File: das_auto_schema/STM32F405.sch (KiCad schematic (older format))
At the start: 11 parts

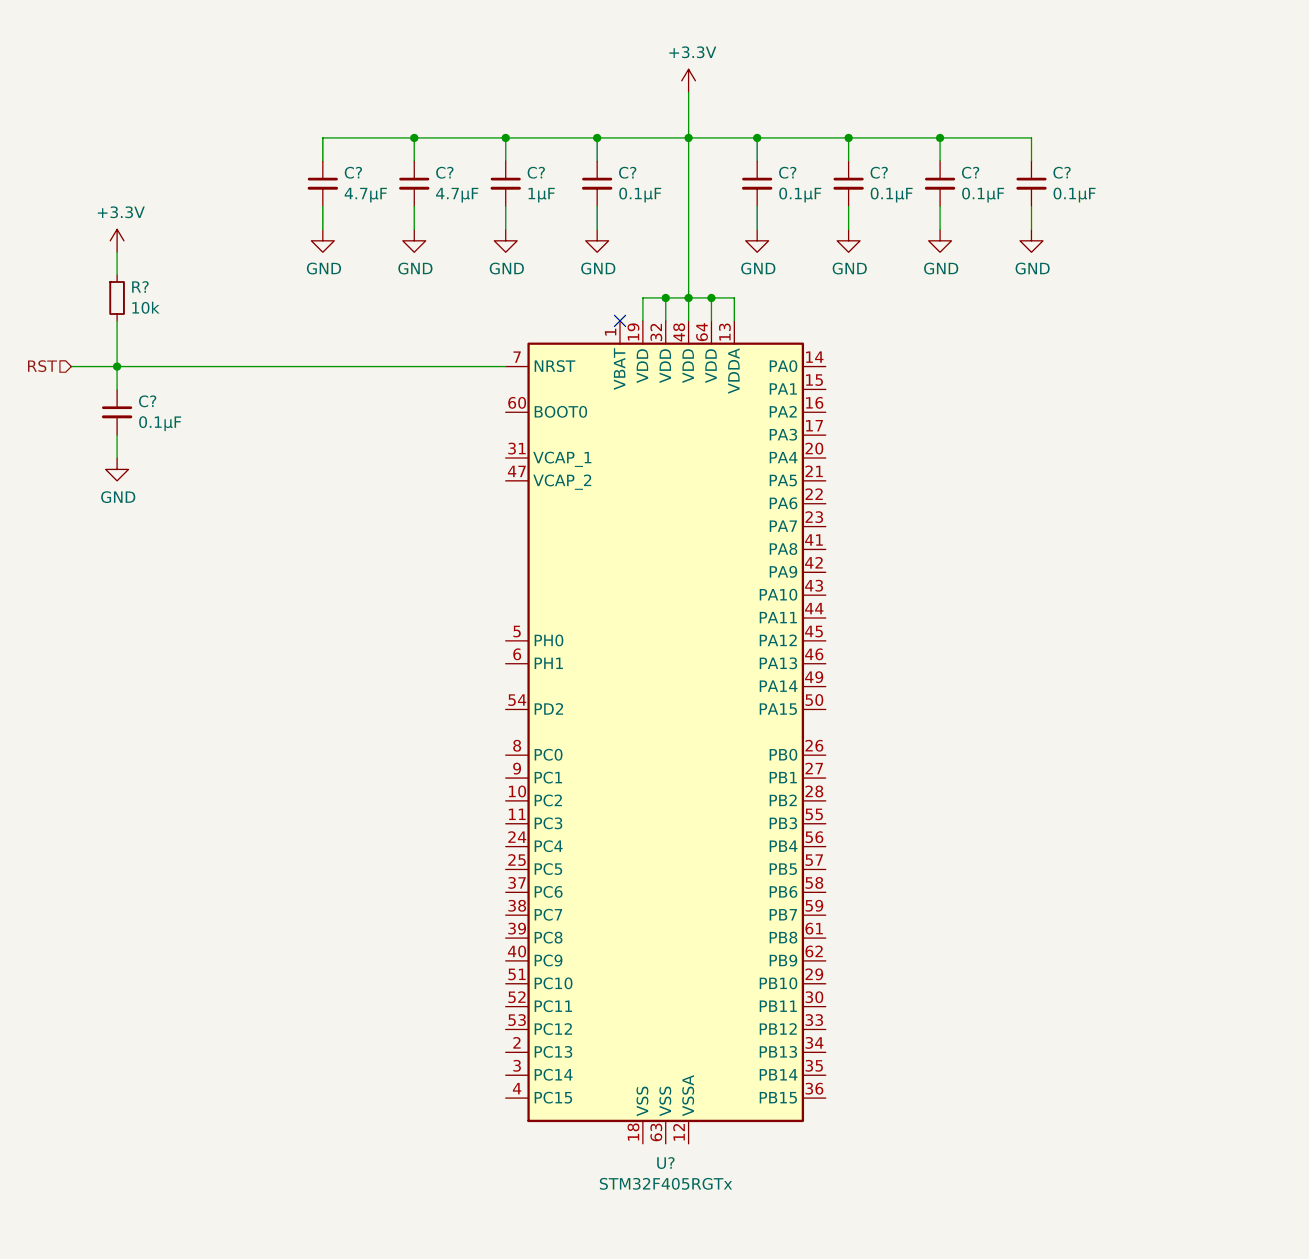
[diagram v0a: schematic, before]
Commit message: Added IMU + python script for realtime plot + Kicad updetes
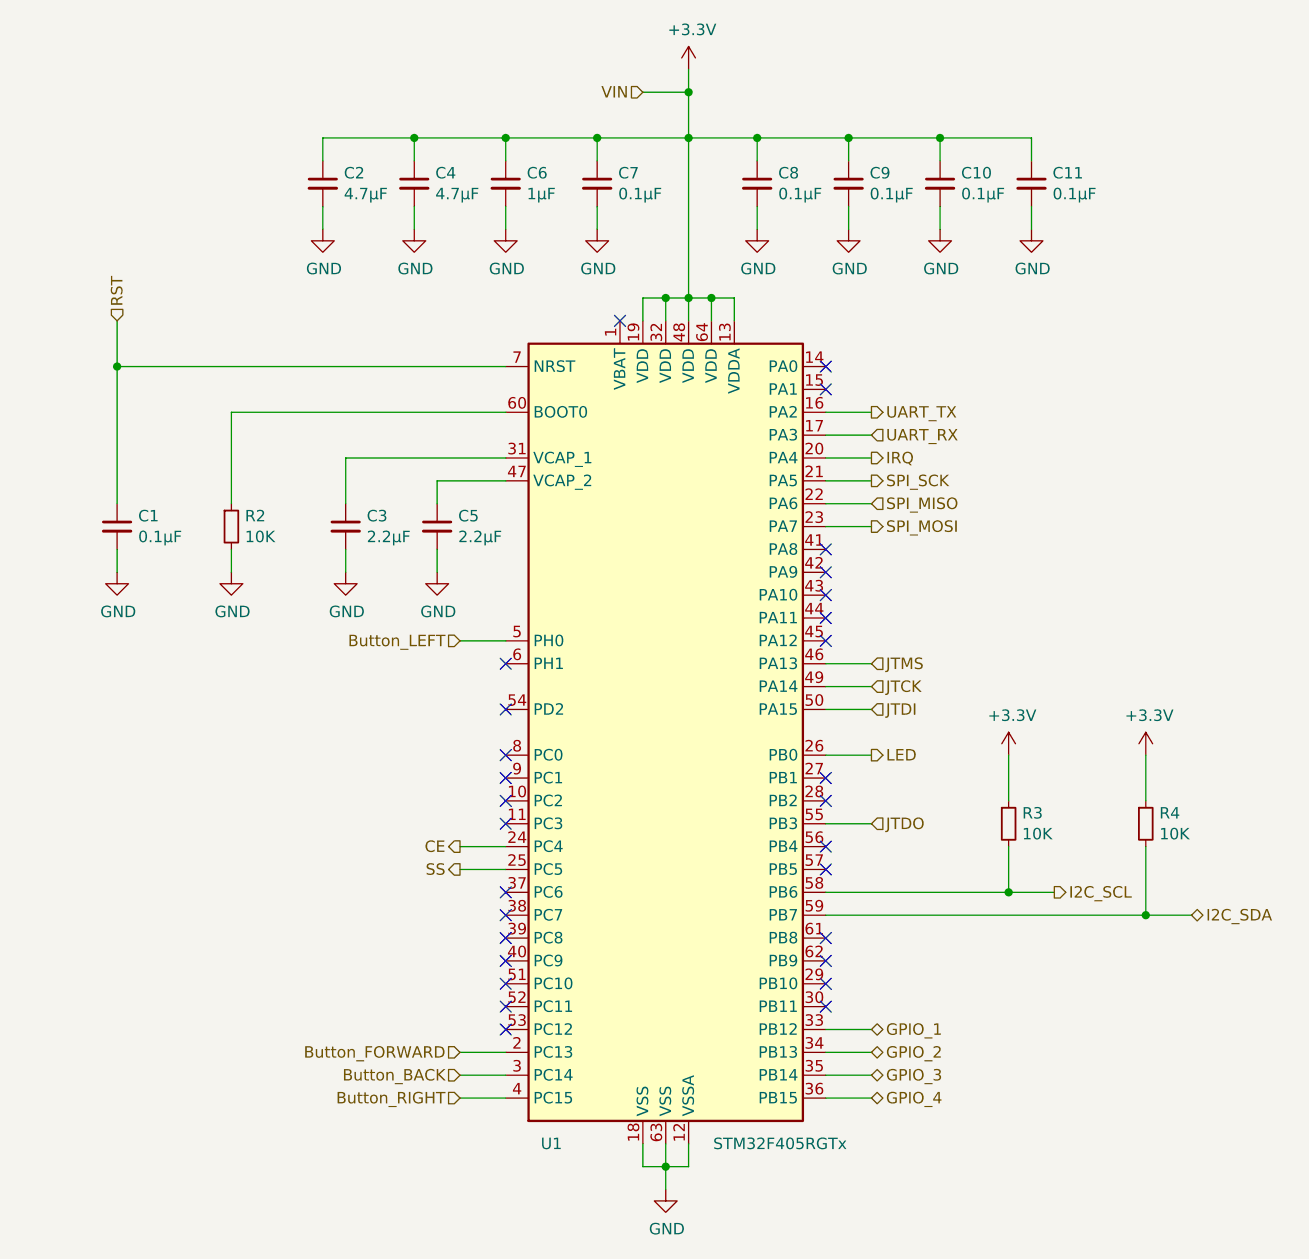
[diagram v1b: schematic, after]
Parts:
- removed R?: 10k, symbol Device:R_Small
- added C3, C5: 2.2µF, Resistor_SMD:R_0805_2012Metric, symbol Device:C_Small
- added R2, R3, R4: 10K, Resistor_SMD:R_0805_2012Metric, symbol Device:R_Small
- C1, C10, C11, C2, C4, C6, C7, C8, C9: renamed from C?; footprint (none) -> Resistor_SMD:R_0805_2012Metric
- gave numbers to parts that had none: 1
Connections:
- net +3V3: now also R3.1, R4.1
- net GND: now also U1.12 (VSSA), U1.18 (VSS), U1.63 (VSS), C3.2, C5.2, R2.2
- net UART_TX: now reaches U1.16 (PA2)
- net UART_RX: now reaches U1.17 (PA3)
- net Button_FORWARD: now reaches U1.2 (PC13)
- net IRQ: now reaches U1.20 (PA4)
- net SPI_SCK: now reaches U1.21 (PA5)
- net SPI_MISO: now reaches U1.22 (PA6)
- net SPI_MOSI: now reaches U1.23 (PA7)
- net CE: now reaches U1.24 (PC4)
- net SS: now reaches U1.25 (PC5)
- net LED: now reaches U1.26 (PB0)
- net Button_BACK: now reaches U1.3 (PC14)
- net at U1.31 (VCAP_1): now also C3.1
- net GPIO_1: now reaches U1.33 (PB12)
- net GPIO_2: now reaches U1.34 (PB13)
- net GPIO_3: now reaches U1.35 (PB14)
- net GPIO_4: now reaches U1.36 (PB15)
- net Button_RIGHT: now reaches U1.4 (PC15)
- net JTMS: now reaches U1.46 (PA13)
- net at U1.47 (VCAP_2): now also C5.1
- net JTCK: now reaches U1.49 (PA14)
- net Button_LEFT: now reaches U1.5 (PH0)
- net JTDI: now reaches U1.50 (PA15)
- net JTDO: now reaches U1.55 (PB3)
- net I2C_SCL: now reaches U1.58 (PB6)
- net I2C_SCL: now also R3.2
- net I2C_SDA: now reaches U1.59 (PB7)
- net I2C_SDA: now also R4.2
- net at U1.60 (BOOT0): now also R2.1
- no-connect marks 1 -> 29
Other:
- moved on the sheet: C1
